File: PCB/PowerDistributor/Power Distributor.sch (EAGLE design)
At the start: 11 parts, among them J3 5.5x2.1mm Barrel

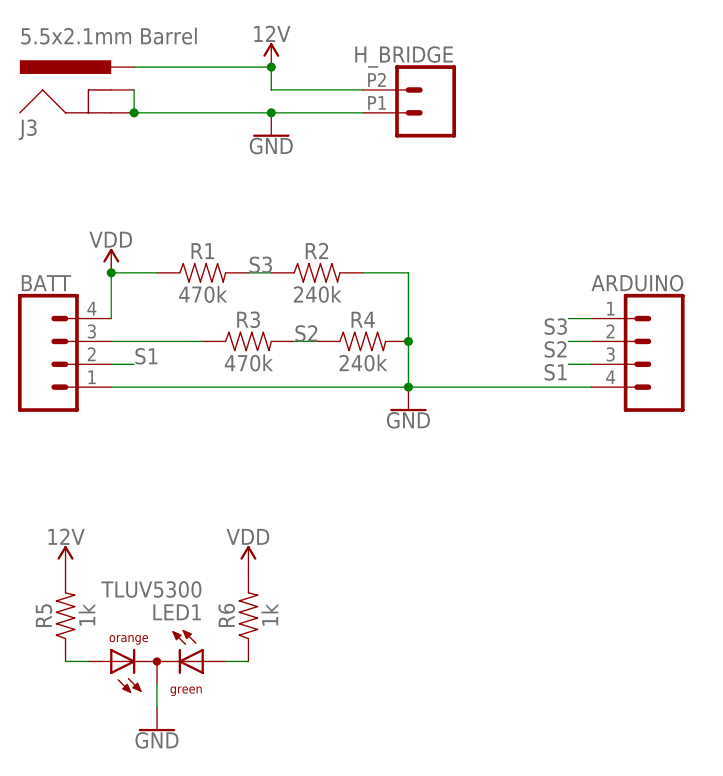
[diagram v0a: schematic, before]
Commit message: update power distributor
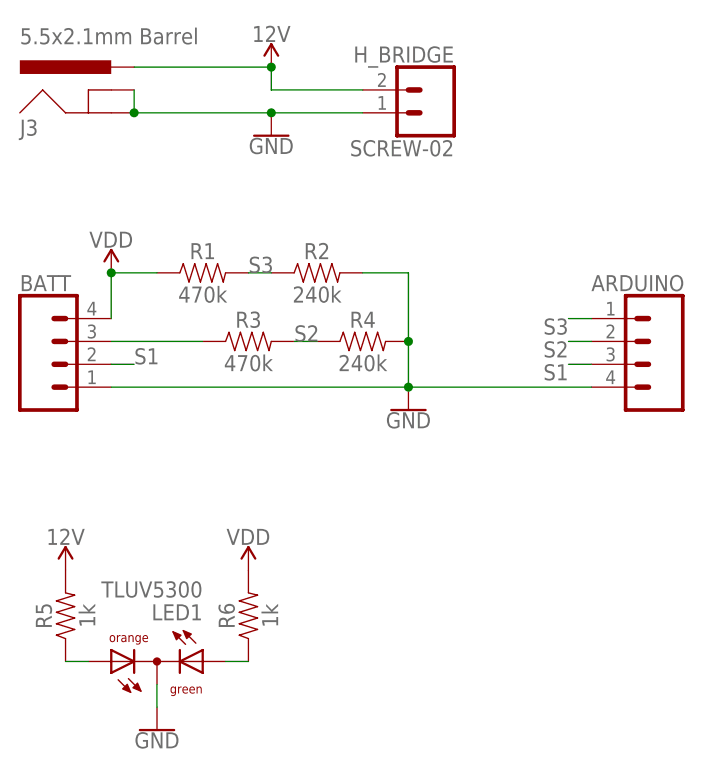
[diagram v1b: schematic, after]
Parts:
- H_BRIDGE: value (none) -> SCREW-02; device SparkFun-Connectors:CONN_022.54MM_SCREWTERM -> KROBOT:SCREW-02
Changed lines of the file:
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@@
 <part name="FRAME1" library="SparkFun-Aesthetics" deviceset="FRAME-A4L" device=""/>
 <part name="BATT" library="KROBOT" deviceset="JST-XH-04-PIN" device="-LONG-PAD"/>
-<part name="H_BRIDGE" library="SparkFun-Connectors" deviceset="CONN_02" device="2.54MM_SCREWTERM"/>
+<part name="H_BRIDGE" library="KROBOT" deviceset="SCREW-02" device=""/>
 <part name="J3" library="SparkFun-Connectors" deviceset="POWER_JACK" device="SMD" value="5.5x2.1mm Barrel"/>
 <part name="R1" library="SparkFun-Resistors" deviceset="RESISTOR" device="1206" value="470k"/>
